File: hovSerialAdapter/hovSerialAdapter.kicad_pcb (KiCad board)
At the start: 2 copper layers, 71.6 x 62.8 mm, 21 parts, among them J2 Ext. Power, J3 54602-908LF, J4 54602-908LF, U1 SN65LVDS179DR, U2 TPS62172DSG

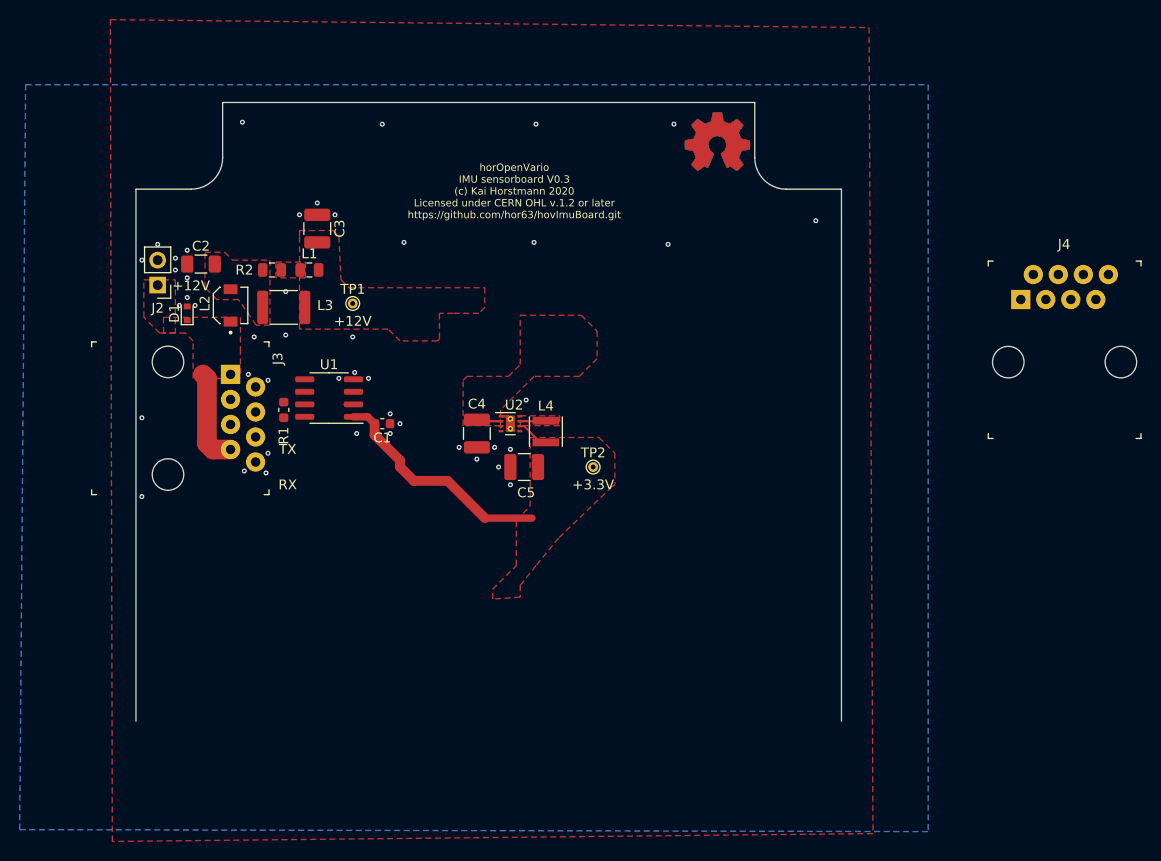
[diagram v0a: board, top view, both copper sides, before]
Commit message: Finalize design of serial adapter board V0.1
Add box symbol and footprint.
Finishing touches on the routings
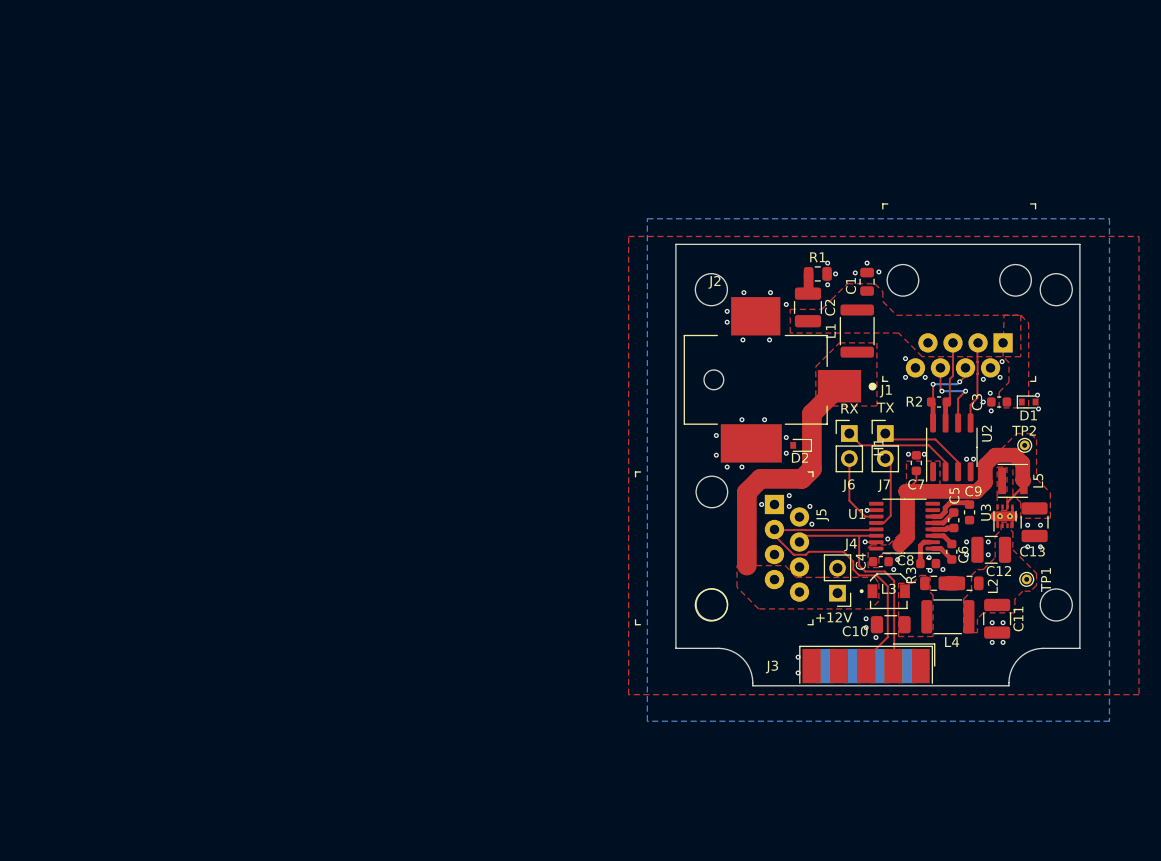
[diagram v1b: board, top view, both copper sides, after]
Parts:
- removed LOGO2: Logo_Open_Hardware_Small, Symbol:OSHW-Symbol_6.7x6mm_Copper
- added C10: 4.7uF, Capacitor_SMD:C_1206_3216Metric, F.Cu at (141.8, 108.8)
- added C11: 22uF, Capacitor_SMD:C_1210_3225Metric, F.Cu at (152.6, 108.2)
- added C12: 22uF, Capacitor_SMD:C_1210_3225Metric, F.Cu at (152.0, 101.2)
- added C13: 22uF, Capacitor_SMD:C_1210_3225Metric, F.Cu at (156.4, 98.4)
- added C6: 100nF, Capacitor_SMD:C_0603_1608Metric, F.Cu at (148.0, 101.4)
- added C7: 100nF, Capacitor_SMD:C_0603_1608Metric, F.Cu at (144.4, 92.4)
- added C8: 100nF, Capacitor_SMD:C_0603_1608Metric, F.Cu at (145.6, 102.6)
- added C9: 100nF, Capacitor_SMD:C_0603_1608Metric, F.Cu at (149.8, 97.4)
- added D2: VESD16C1-02V-G3-08, Diode_SMD:D_SOD-523, F.Cu at (132.6, 90.6)
- added H1: Box, hovImuBoard:Box-MB655030, F.Cu at (141.1, 90.8)
- added J1: 54602-908LF, hovImuBoard:Ethernet_Jack_54602-908LF, F.Cu at (153.2, 80.2)
- added J5: 54602-908LF, hovImuBoard:Ethernet_Jack_54602-908LF, F.Cu at (130.0, 96.6)
- added J6: RX, Connector_PinHeader_2.54mm:PinHeader_1x02_P2.54mm_Vertical, F.Cu at (137.6, 89.4)
- added J7: TX, Connector_PinHeader_2.54mm:PinHeader_1x02_P2.54mm_Vertical, F.Cu at (141.2, 89.4)
- added L5: 2.2uH, hovImuBoard:IND_LQH3NPN2R2MMEL, F.Cu at (154.2, 94.2)
- added R3: 180m, Resistor_SMD:R_0805_2012Metric, F.Cu at (146.2, 104.6)
- added U3: TPS62172DSG, Package_SON:WSON-8-1EP_2x2mm_P0.5mm_EP0.9x1.6mm_ThermalVias, F.Cu at (153.4, 97.8)
- C1: value 100nF -> 2.2uF; footprint Capacitor_SMD:C_0603_1608Metric -> Capacitor_SMD:C_0805_2012Metric
- C2: value 4.7uF -> 22uF; footprint Capacitor_SMD:C_1206_3216Metric -> Capacitor_SMD:C_1210_3225Metric
- C3, C4, C5: value 22uF -> 100nF; footprint Capacitor_SMD:C_1210_3225Metric -> Capacitor_SMD:C_0603_1608Metric
- J2: value Ext. Power -> Power jack; footprint Connector_PinHeader_2.54mm:PinHeader_1x02_P2.54mm_Vertical -> hovImuBoard:CUI_PJ-036AH-SMT-TR
- J3: value 54602-908LF -> DB9_Female; footprint hovImuBoard:Ethernet_Jack_54602-908LF -> Connector_Dsub:DSUB-9_Female_EdgeMount_P2.77mm
- J4: value 54602-908LF -> Ext. Power; footprint hovImuBoard:Ethernet_Jack_54602-908LF -> Connector_PinHeader_2.54mm:PinHeader_1x02_P2.54mm_Vertical
- L1: value 240nH -> 4.7uH; footprint Inductor_SMD:L_0805_2012Metric -> Inductor_SMD:L_1812_4532Metric
- L2: value 1.2uH -> 240nH; footprint hovImuBoard:IND_1231AS-H-1R2N=P3 -> Inductor_SMD:L_0805_2012Metric
- L3: value 8.2uH -> 1.2uH; footprint Inductor_SMD:L_1812_4532Metric -> hovImuBoard:IND_1231AS-H-1R2N=P3
- L4: value 2.2uH -> 8.2uH; footprint hovImuBoard:IND_LQH3NPN2R2MMEL -> Inductor_SMD:L_1812_4532Metric
- LOGO1: footprint Symbol:OSHW-Symbol_6.7x6mm_Copper -> Symbol:OSHW-Symbol_6.7x6mm_SilkScreen; moved to B.Cu
- R1: value 100 -> 1.5; footprint Resistor_SMD:R_0603_1608Metric -> Resistor_SMD:R_0805_2012Metric
- R2: value 180m -> 100; footprint Resistor_SMD:R_0805_2012Metric -> Resistor_SMD:R_0603_1608Metric
- U1: value SN65LVDS179DR -> MAX3232; footprint Package_SO:SOIC-8_3.9x4.9mm_P1.27mm -> Package_SO:TSSOP-16_4.4x5mm_P0.65mm
- U2: value TPS62172DSG -> SN65LVDS179DR; footprint Package_SON:WSON-8-1EP_2x2mm_P0.5mm_EP0.9x1.6mm_ThermalVias -> Package_SO:SOIC-8_3.9x4.9mm_P1.27mm
- moved D1 85.9 mm to (155.8, 86.2), turned to 0 degrees
- moved L2 80.1 mm to (149.8, 104.6), turned to 0 degrees
- moved TP1 73.9 mm to (155.6, 104.2)
- moved C3 71.4 mm to (152.8, 86.2), turned to 180 degrees
- moved J3 71.0 mm to (139.3, 113.0), turned to 0 degrees
- moved J2 70.0 mm to (136.6, 84.6), turned to 0 degrees
- moved R2 69.0 mm to (146.7, 86.2), turned to 180 degrees
- moved L3 67.8 mm to (141.6, 105.4)
- moved C2 61.8 mm to (133.4, 76.6), turned to 270 degrees
- moved U1 59.8 mm to (143.2, 98.8)
- moved L1 55.9 mm to (138.4, 79.0), turned to 90 degrees
- moved R1 55.9 mm to (134.4, 73.2), turned to 0 degrees
- moved LOGO1 52.4 mm to (145.9, 107.5)
- moved C1 51.3 mm to (139.4, 74.0), turned to 270 degrees
- moved L4 44.9 mm to (147.6, 108.0), turned to 0 degrees
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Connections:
- C1 pad 2: +3V3 -> VBUS
- C2 pad 1: GND -> Net-(C2-Pad1)
- C2 pad 2: Net-(C2-Pad2) -> VBUS
- C3 pad 1: GND -> VBUS
- C3 pad 2: +12V -> GND
- C4 pad 1: GND -> +3V3
- C4 pad 2: +12V -> GND
- C5 pad 1: GND -> Net-(C5-Pad1)
- C5 pad 2: +3V3 -> Net-(C5-Pad2)
- D1 pad 1: +VDC -> VBUS
- J3 pad 1: +VDC -> (no net)
- J3 pad 2: GND -> /TX_RS232
- J3 pad 3: /TX+ -> /RX_RS232
- J3 pad 4: /RX+ -> (no net)
- J3 pad 5: /RX- -> GND
- J3 pad 6: /TX- -> (no net)
- J3 pad 7: +VDC -> (no net)
- J3 pad 8: GND -> (no net)
- J4 pad 1: (no net) -> +VDC
- J4 pad 2: (no net) -> GND
- L1 pad 1: Net-(L1-Pad1) -> +VDC
- L1 pad 2: +12V -> VBUS
- L2 pad 1: +VDC -> Net-(L2-Pad1)
- L2 pad 2: Net-(C2-Pad2) -> +12V
- L3 pad 1: Net-(C2-Pad2) -> +VDC
- L3 pad 2: +12V -> Net-(C10-Pad2)
- L4 pad 1: Net-(L4-Pad1) -> Net-(C10-Pad2)
- L4 pad 2: +3V3 -> +12V
- R1 pad 1: /RX+ -> Net-(C2-Pad1)
- R1 pad 2: /RX- -> GND
- R2 pad 1: Net-(C2-Pad2) -> /RX-
- R2 pad 2: Net-(L1-Pad1) -> /RX+
- U1 pad 1: +3V3 -> Net-(C6-Pad1)
- U1 pad 2: (no net) -> Net-(C8-Pad2)
- U1 pad 3: (no net) -> Net-(C6-Pad2)
- U1 pad 4: GND -> Net-(C5-Pad2)
- U1 pad 5: /TX+ -> Net-(C5-Pad1)
- U1 pad 6: /TX- -> Net-(C9-Pad1)
- U1 pad 7: /RX- -> Net-(U1-Pad7)
- U1 pad 8: /RX+ -> Net-(U1-Pad7)
- U2 pad 1: GND -> +3V3
- U2 pad 2: +12V -> /RX_LVDS
- U2 pad 3: (no net) -> /TX_LVDS
- U2 pad 5: GND -> /TX+
- U2 pad 6: +3V3 -> /TX-
- U2 pad 7: Net-(L4-Pad1) -> /RX-
- U2 pad 8: (no net) -> /RX+
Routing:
- net /RX_RS232: track 0.00 -> 34.4 mm
- net /TX_RS232: track 0.00 -> 24.0 mm
- net +VDC: track 9.82 -> 24.6 mm
- net /RX_LVDS: track 0.00 -> 11.9 mm
- net /TX_LVDS: track 0.00 -> 9.61 mm
- net /RX+: track 0.00 -> 8.54 mm, vias 0 -> 2
- net /TX+: track 0.00 -> 8.45 mm
- net /TX-: track 0.00 -> 8.36 mm, vias 0 -> 2
- net /RX-: track 0.37 -> 8.44 mm
- net /TX: track 0.00 -> 7.80 mm
- net /RX: track 0.00 -> 7.68 mm
- net GND: track 1.05 -> 8.17 mm, vias 45 -> 66
- net Net-(C9-Pad1): track 0.00 -> 4.64 mm
- net Net-(C8-Pad2): track 0.00 -> 2.94 mm
- net Net-(L4-Pad1): track 2.67 -> 0.00 mm
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- added copper zone on F.Cu, net Net-(C10-Pad2)
- added copper zone on F.Cu, net Net-(L5-Pad1)
- added copper zone on F.Cu, net VBUS
- removed copper zone on F.Cu, net Net-(C2-Pad2)
- removed copper zone on F.Cu, net Net-(L1-Pad1)
- removed copper zone on F.Cu, net Net-(L4-Pad1)
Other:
- board size 71.6 x 62.8 mm -> 41 x 44.8 mm
- board text added: "horOpenVario IMU sensorboard serial converter (c) Kai Horstmann 2020 Licensed under CERN OHL v.1.2 or later https://github.com/hor63/hovImuBoard.git"
- board text removed: "horOpenVario IMU sensorboard V0.3 (c) Kai Horstmann 2020 Licensed under CERN OHL v.1.2 or later https://github.com/hor63/hovImuBoard.git"

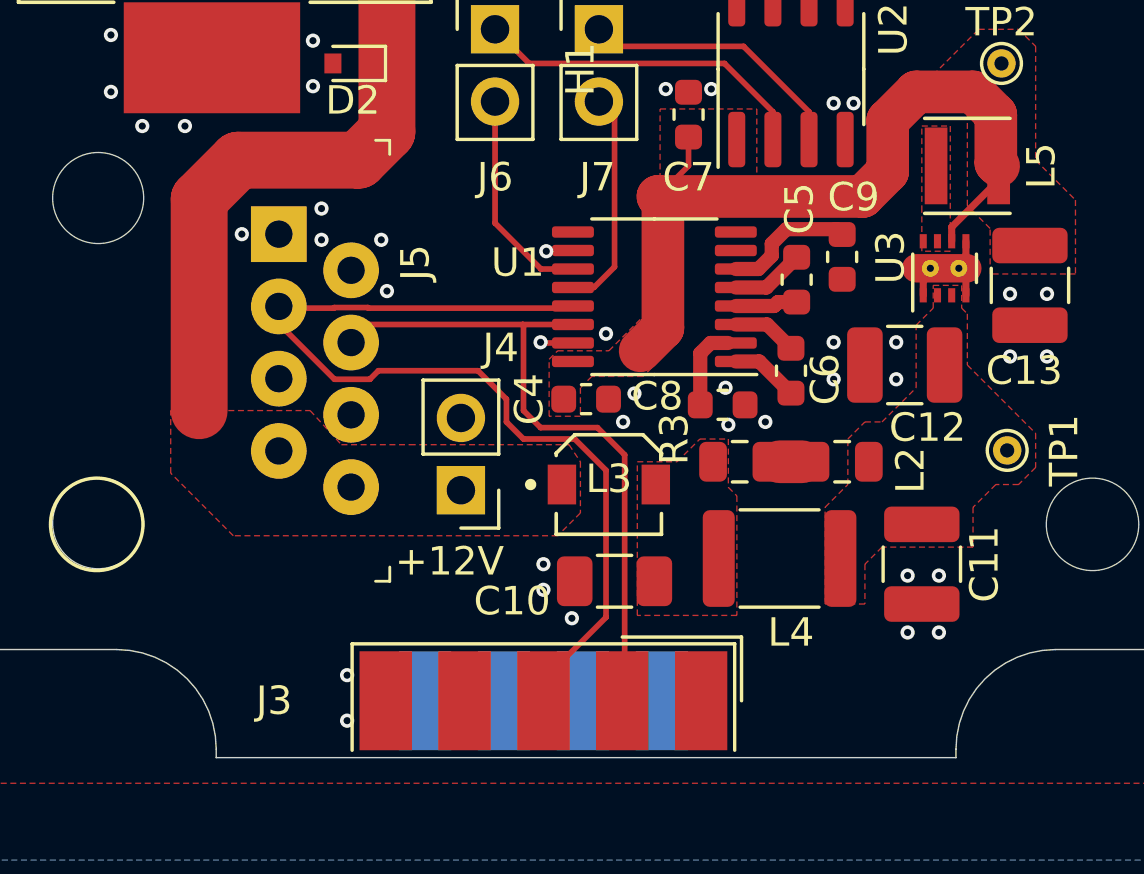
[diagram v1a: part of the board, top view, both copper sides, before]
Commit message: hovSerialAdapter: Add 3D models from SnapEDA.
Add 3D models from SnapEDA to the footprints of the RJ-45 jack, and for the 8.2uH inductivity
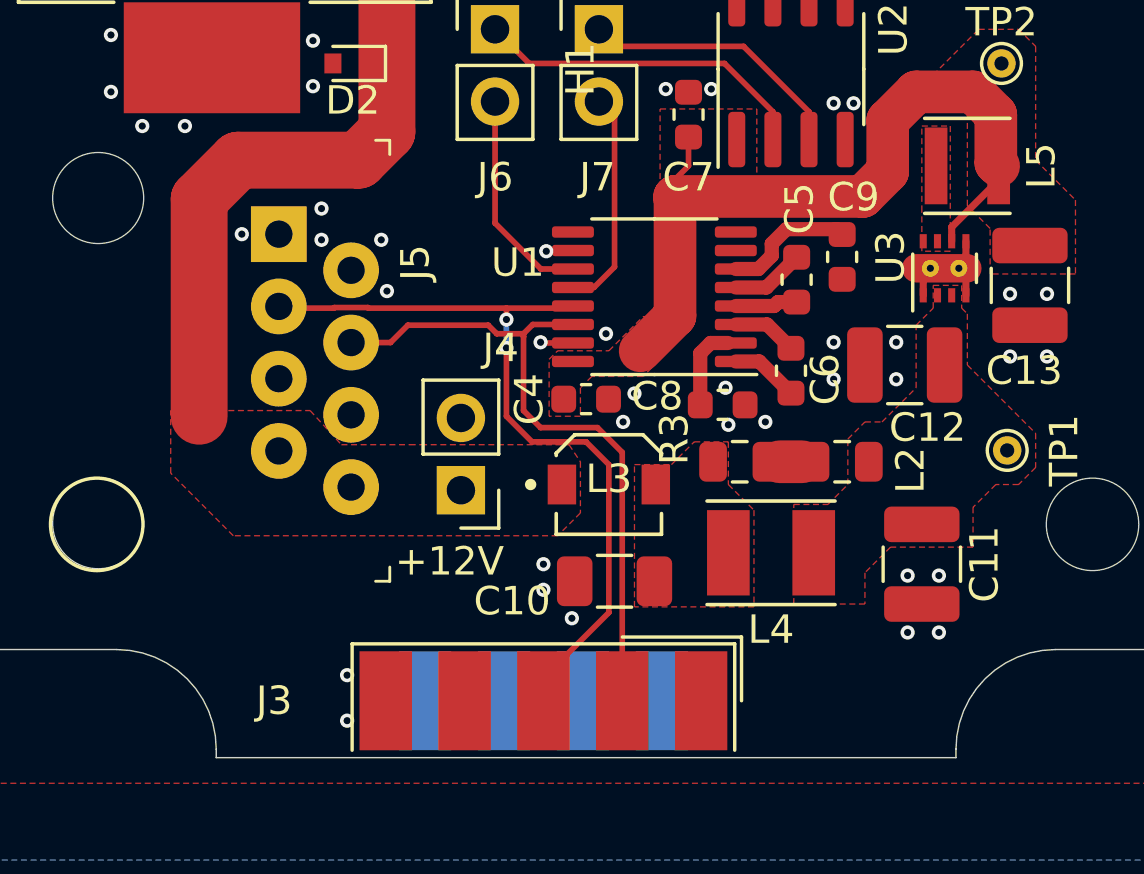
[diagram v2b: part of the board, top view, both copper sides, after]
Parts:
- L4: footprint Inductor_SMD:L_1812_4532Metric -> hovImuBoard:IND_LQH43PH8R2M26L
- moved L4 0.36 mm to (147.3, 107.8)
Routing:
- net /RX_RS232: track 34.4 -> 27.8 mm, vias 0 -> 2
- net +12V: track 0.00 -> 0.75 mm

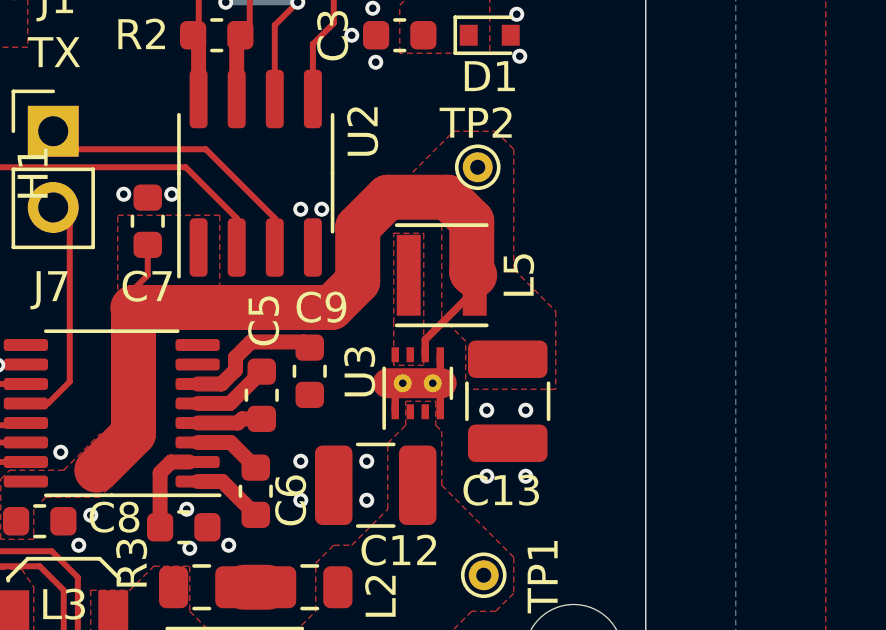
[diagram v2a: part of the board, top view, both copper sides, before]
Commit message: hovSerialAdapter: Add 3D model for the D-Sub connector.
Copy the footprint to lib/hovImuBoard.pretty, and add the 3D model.
Improve the switching trace on the 3.3V regulator, moving the feedback further out of the way
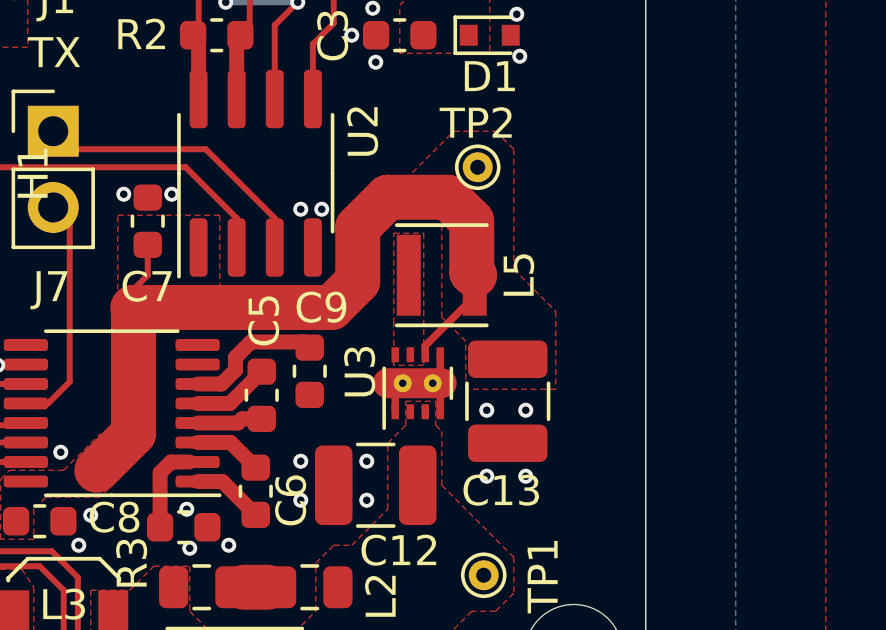
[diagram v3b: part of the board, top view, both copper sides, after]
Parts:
- J3: footprint Connector_Dsub:DSUB-9_Female_EdgeMount_P2.77mm -> hovImuBoard:DSUB-9_Female_EdgeMount_P2.77mm

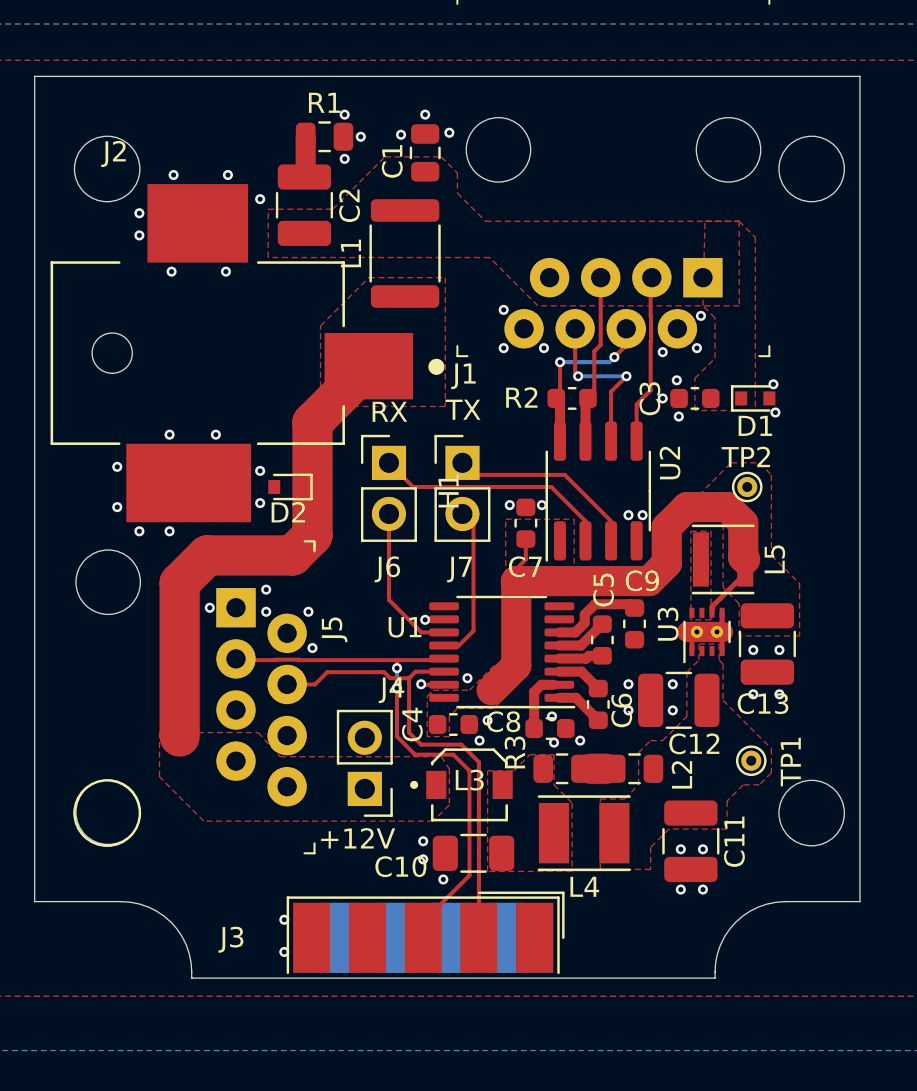
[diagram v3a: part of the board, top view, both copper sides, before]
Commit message: Conversion to KiCad 6.0, add 3D models
First commit after successful conversion.
Save first before cleanup of outdated KiCad 5 files. Just to be sure.

Added missing 3D models for various parts. Downloaded from SNAP-EDA or
directly from the manufacturer's site.
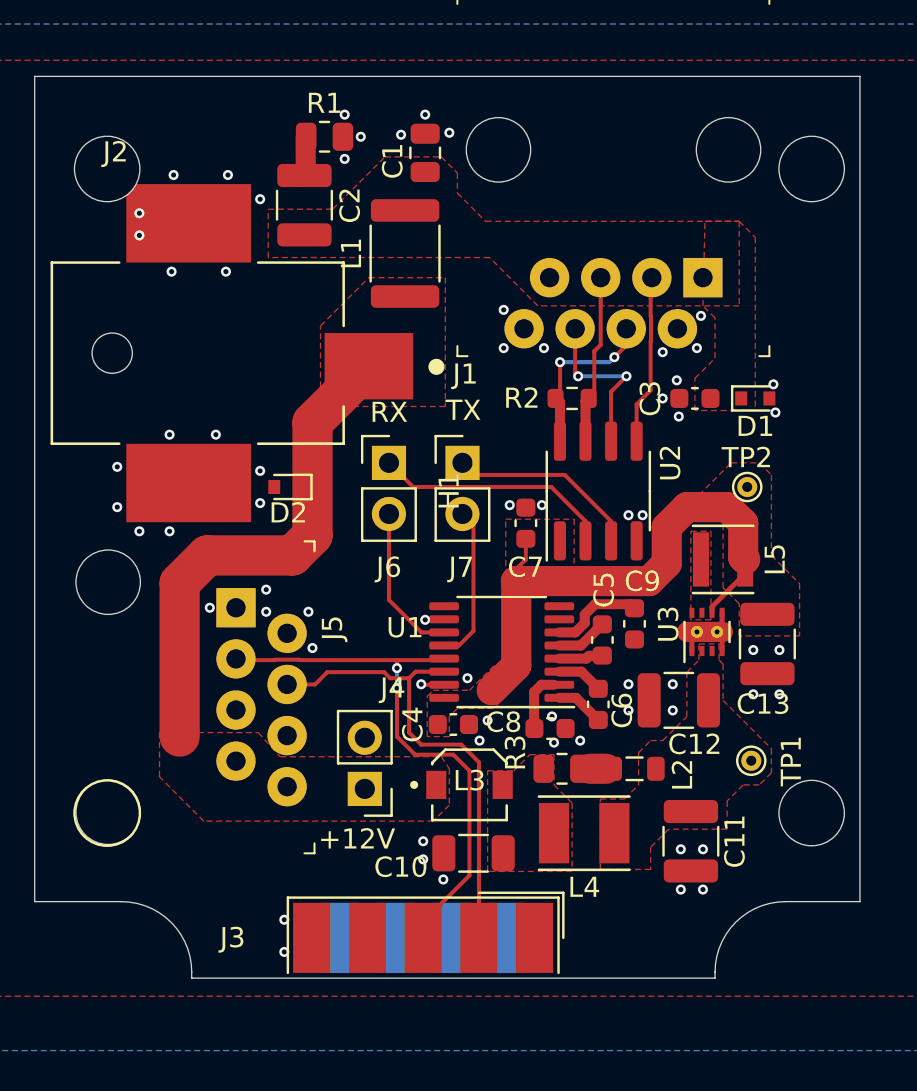
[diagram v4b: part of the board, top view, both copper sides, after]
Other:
- net class Default removed
- net class PWR2Pad removed
- net class Signal removed
